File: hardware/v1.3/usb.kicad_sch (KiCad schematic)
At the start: 47 parts, among them J3 USB_C_Receptacle_USB2.0_14P, J4 USB_C_Receptacle_USB2.0_14P, J5 USB_C_Receptacle_USB2.0_14P, U1 ECP5-CABGA256, U6 FT231XQ, U7 TPD2EUSB30A, U8 TPD2EUSB30A, U9 TPD2EUSB30A

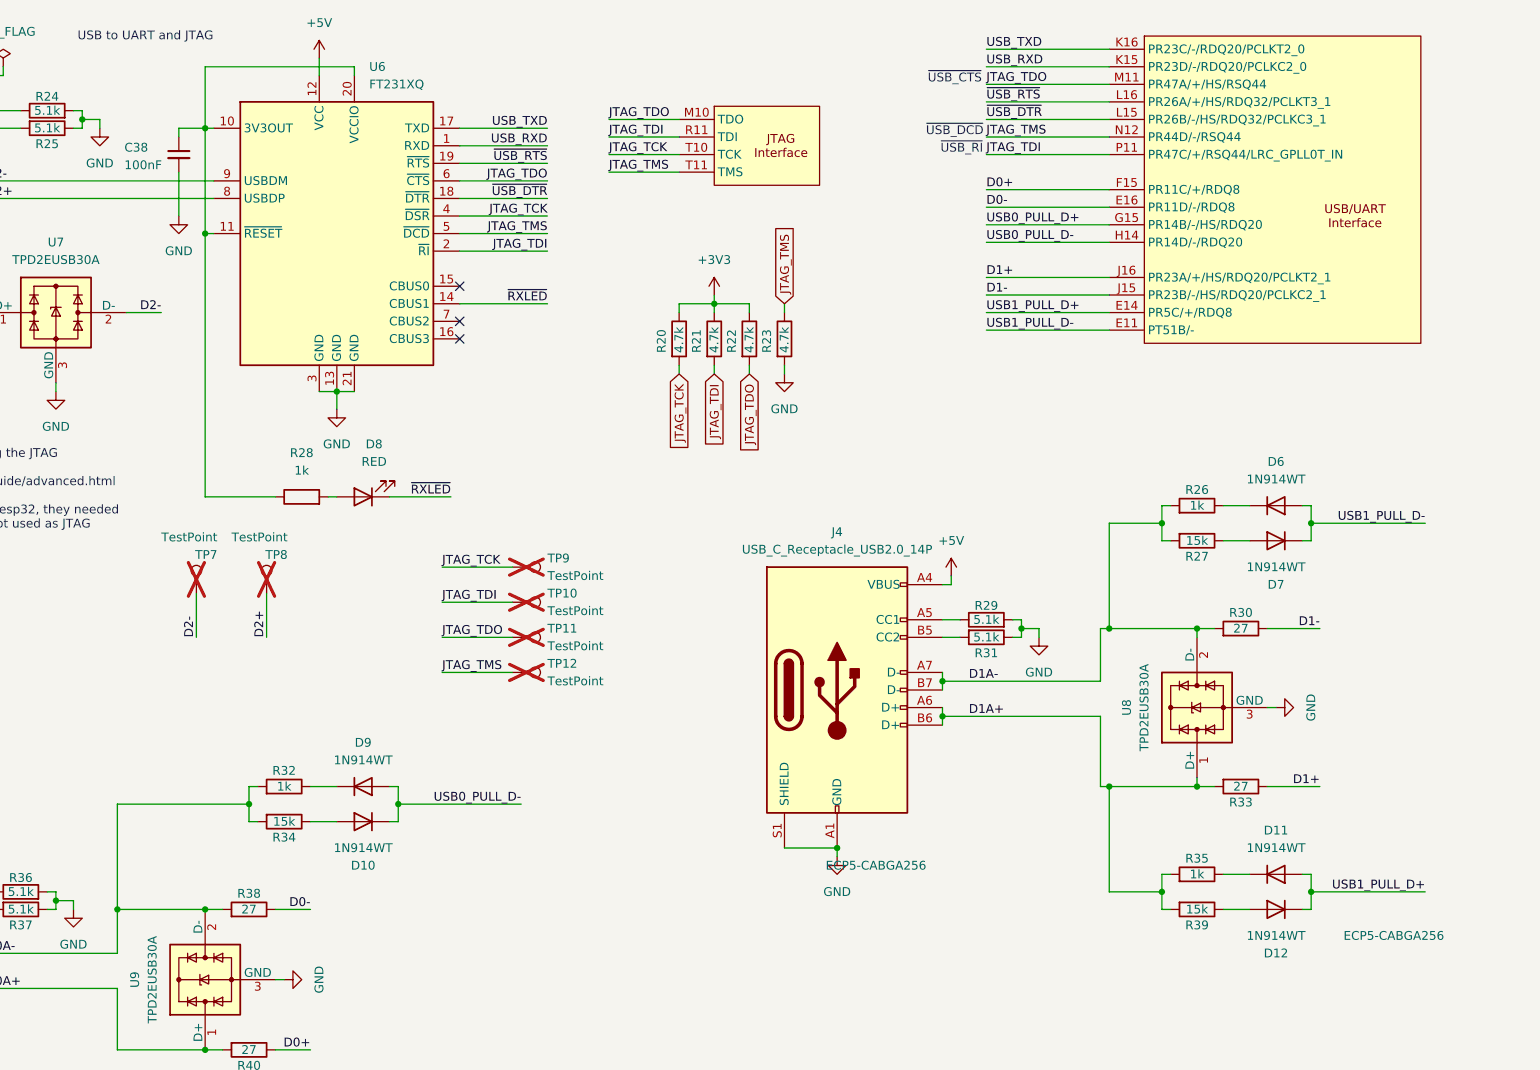
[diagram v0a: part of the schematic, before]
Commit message: Refine README
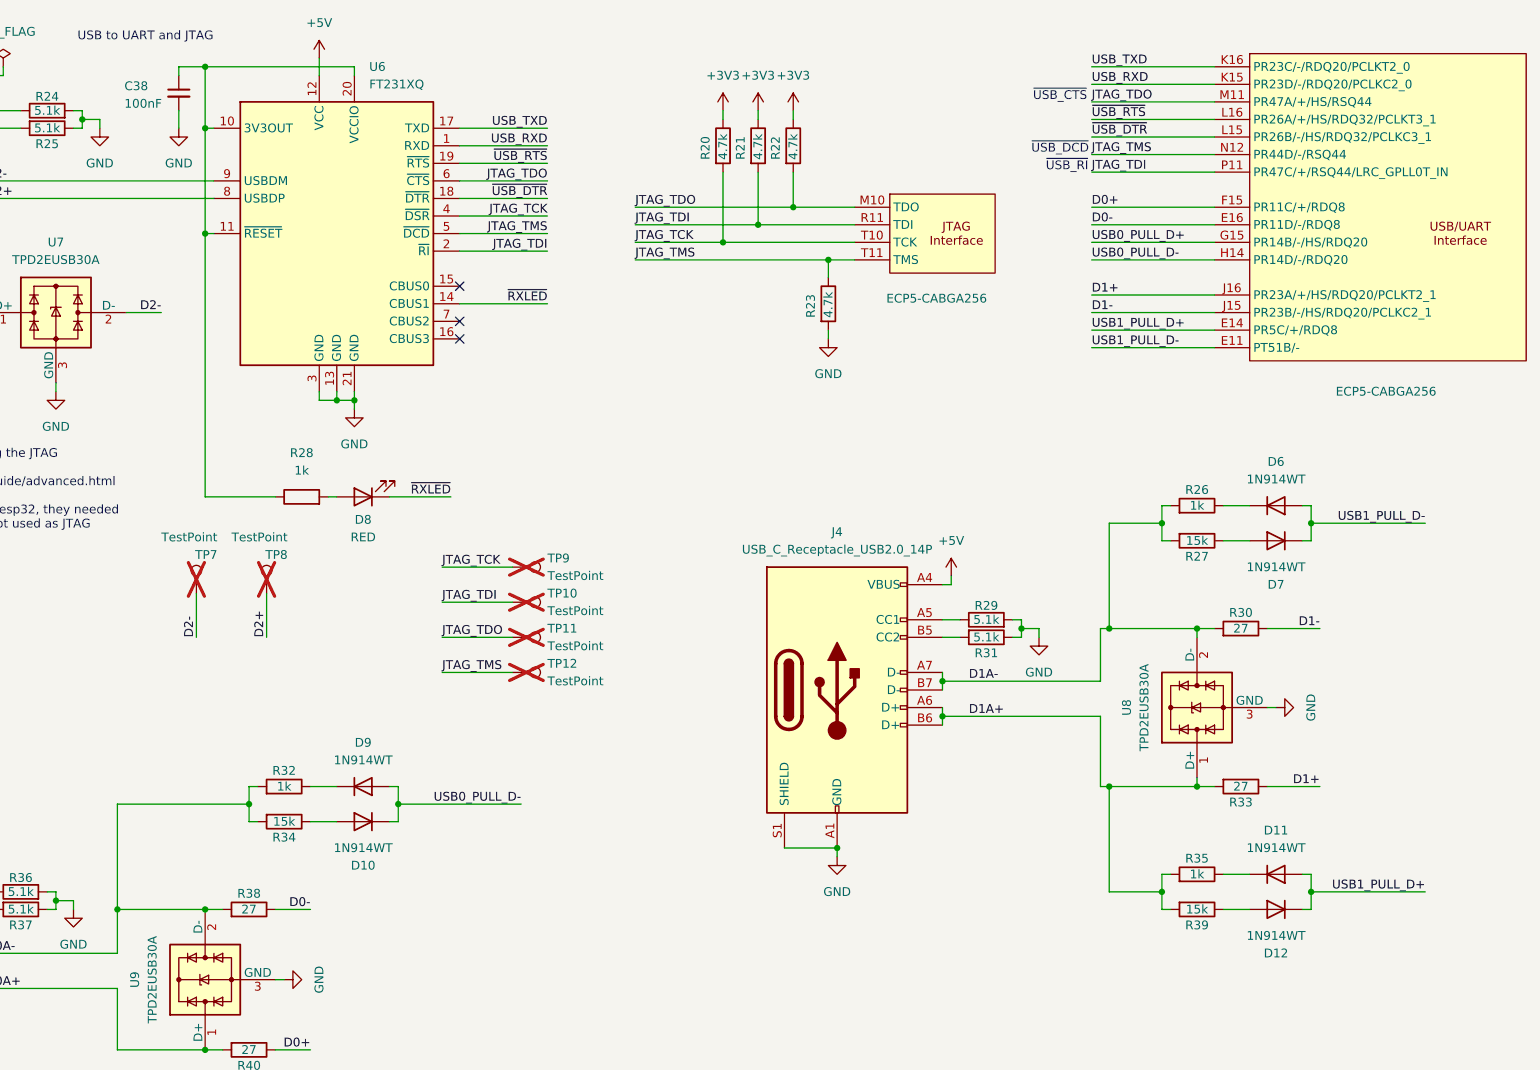
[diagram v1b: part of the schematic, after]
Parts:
- C38: LCSC Link (none) -> https://lcsc.com/product-detail/Multilayer-Ceramic-Capacito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; LCSC Part # C307331 -> C307331; Manufactuer Part Number (none) -> CL05B104KB54PNC
- D10, D11, D12, D13, D14, D6, D7, D9: LCSC Link (none) -> https://lcsc.com/product-detail/Switching-Diodes_CBI-1N914W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; Manufactuer Part Number (none) -> 1N914WT
- D8: LCSC Link (none) -> https://lcsc.com/product-detail/LED-Indication-Discrete_Hub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; LCSC Part # C2286 -> C2286; Manufactuer Part Number (none) -> KT-0603R
- J3, J4, J5: LCSC Link (none) -> https://lcsc.com/product-detail/USB-Connectors_SHOU-HAN-TYP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; Manufactuer Part Number (none) -> TYPE-C 16PIN 2MD(073)
- R20, R21, R22, R23: LCSC Link (none) -> https://lcsc.com/product-detail/Chip-Resistor-Surface-Mount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; LCSC Part # C25900 -> C25900; Manufactuer Part Number (none) -> 0402WGF4701TCE
- R24, R25, R29, R31, R36, R37: LCSC Link (none) -> https://lcsc.com/product-detail/Chip-Resistor-Surface-Mount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; LCSC Part # C25905 -> C25905; Manufactuer Part Number (none) -> 0402WGF5101TCE
- R26, R28, R32, R35, R41: LCSC Link (none) -> https://lcsc.com/product-detail/Chip-Resistor-Surface-Mount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; Manufactuer Part Number (none) -> 0402WGF1001TCE
- R27, R34, R39, R42: LCSC Link (none) -> https://lcsc.com/product-detail/Chip-Resistor-Surface-Mount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; Manufactuer Part Number (none) -> 0402WGF1502TCE
- R30, R33, R38, R40: LCSC Link (none) -> https://lcsc.com/product-detail/Chip-Resistor-Surface-Mount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; Manufactuer Part Number (none) -> 0201WMF270JTEE
- U1: LCSC Link (none) -> https://lcsc.com/product-detail/Programmable-Logic-Device-C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; LCSC Part # (none) -> C1521614; Manufactuer Part Number (none) -> LFE5U-25F-6BG256C
- U6: LCSC Link (none) -> https://lcsc.com/product-detail/USB-Converters_FTDI-FT231XQ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; Manufactuer Part Number (none) -> FT231XQ-R
- U7, U8, U9: LCSC Link (none) -> https://lcsc.com/product-detail/ESD-and-Surge-Protection-TV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; Manufactuer Part Number (none) -> TPD2EUSB30ADRTR
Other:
- moved on the sheet: C38, R20, R21, R22, R23

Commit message: DVI multires
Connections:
- net JTAG_TDI: no longer U1.P11 (PR47C/+/RSQ44/LRC_GPLL0T_IN)
- net JTAG_TDO: no longer U1.M11 (PR47A/+/HS/RSQ44)
- net JTAG_TMS: no longer U1.N12 (PR44D/-/RSQ44)
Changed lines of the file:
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@@
-	(wire
-		(pts
-			(xy 218.44 31.75) (xy 236.22 31.75)
-		)
-		(stroke
-			(width 0)
-			(type default)
-		)
-	)
 	(wire
 		(pts
@@
 		)
 		(stroke
-			(width 0)
-			(type default)
-		)
-	)
-	(wire
-		(pts
-			(xy 218.44 39.37) (xy 236.22 39.37)
-		)
-		(stroke
-			(width 0)
-			(type default)
-		)
-	)
-	(wire
-		(pts
-			(xy 218.44 41.91) (xy 236.22 41.91)
-		)
-		(stroke

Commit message: Update files
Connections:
- no-connect marks 3 -> 6
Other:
- note added: "FPGA-TN-02039 specified pull resistors"
- note added: "The FTDI chip can bitbang the JTAG output on any pin UART: https://umarcor.github.io/openFPGALoader/guide/advanced.html"
- note removed: "The FTDI chip can probably bit bang the JTAG output on any pin: https://umarcor.github.io/openFPGALoader/guide/advanced.html ULX chose the pins because to program their esp32, they needed specific uart outputs, and the ones left got used as JTAG"
- note removed: "~{USB_CTS}"
- note removed: "~{USB_DCD}"
- note removed: "~{USB_RI}"
- moved on the sheet: C38, D10, D11, D12, D13, D14, D6, D7, D8, D9, J3, J4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

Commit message: Update to v1.3 board
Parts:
- TP10, TP11, TP12, TP7, TP8, TP9: now left out of the parts list

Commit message: Final mass production files
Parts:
- added C37: 22uF, Capacitor_SMD:C_0603_1608Metric, symbol Device:C
- TP10, TP11, TP12, TP9: footprint TestPoint:TestPoint_Pad_D1.0mm -> icepi-lib:TestPoint_Pad_D1.0mm_Blank
- TP7, TP8: footprint TestPoint:TestPoint_Pad_D2.0mm -> icepi-lib:TestPoint_Pad_D2.0mm_Blank
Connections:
- net +5V: now also C37.1
- net GND: now also C37.2
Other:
- note added: "PWRin (bulk?) decoupling"
- moved on the sheet: D10, D13, D14, D9, J5, R32, R34, R36, R37, R38, R40, R41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

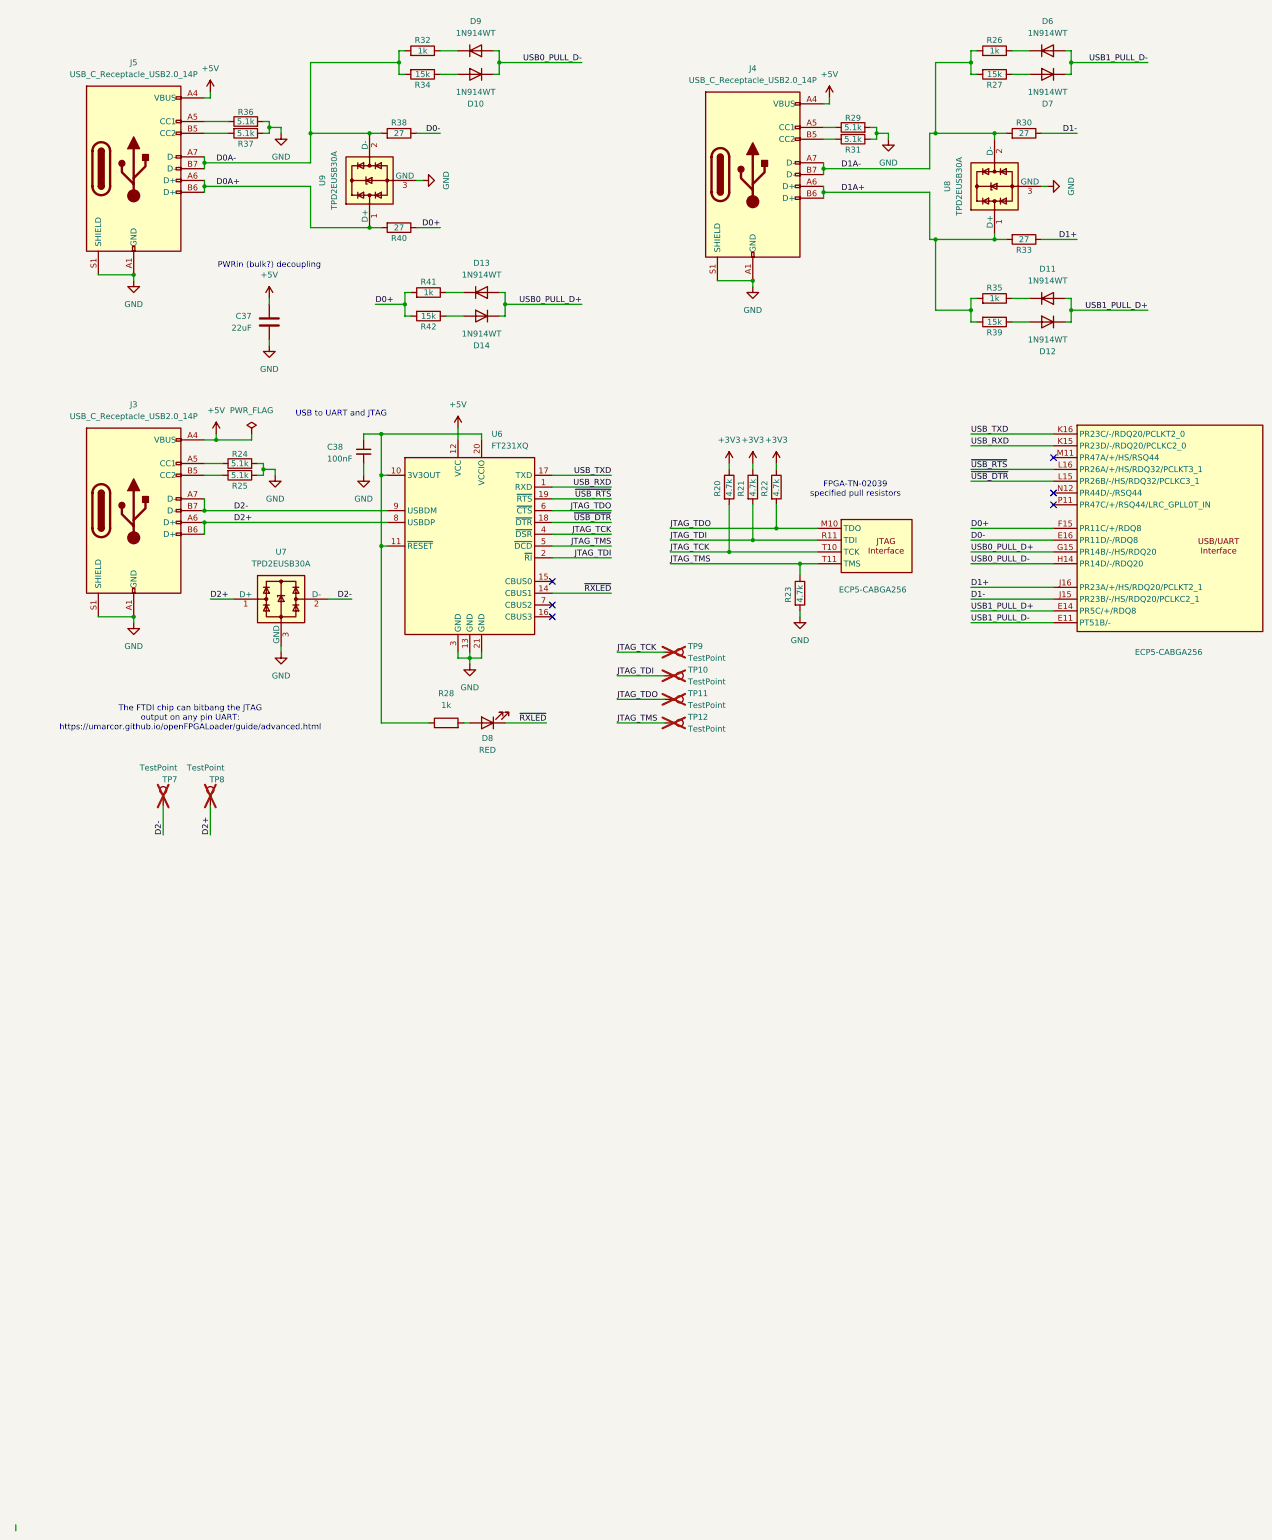
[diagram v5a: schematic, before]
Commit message: Improve makefile and hardware
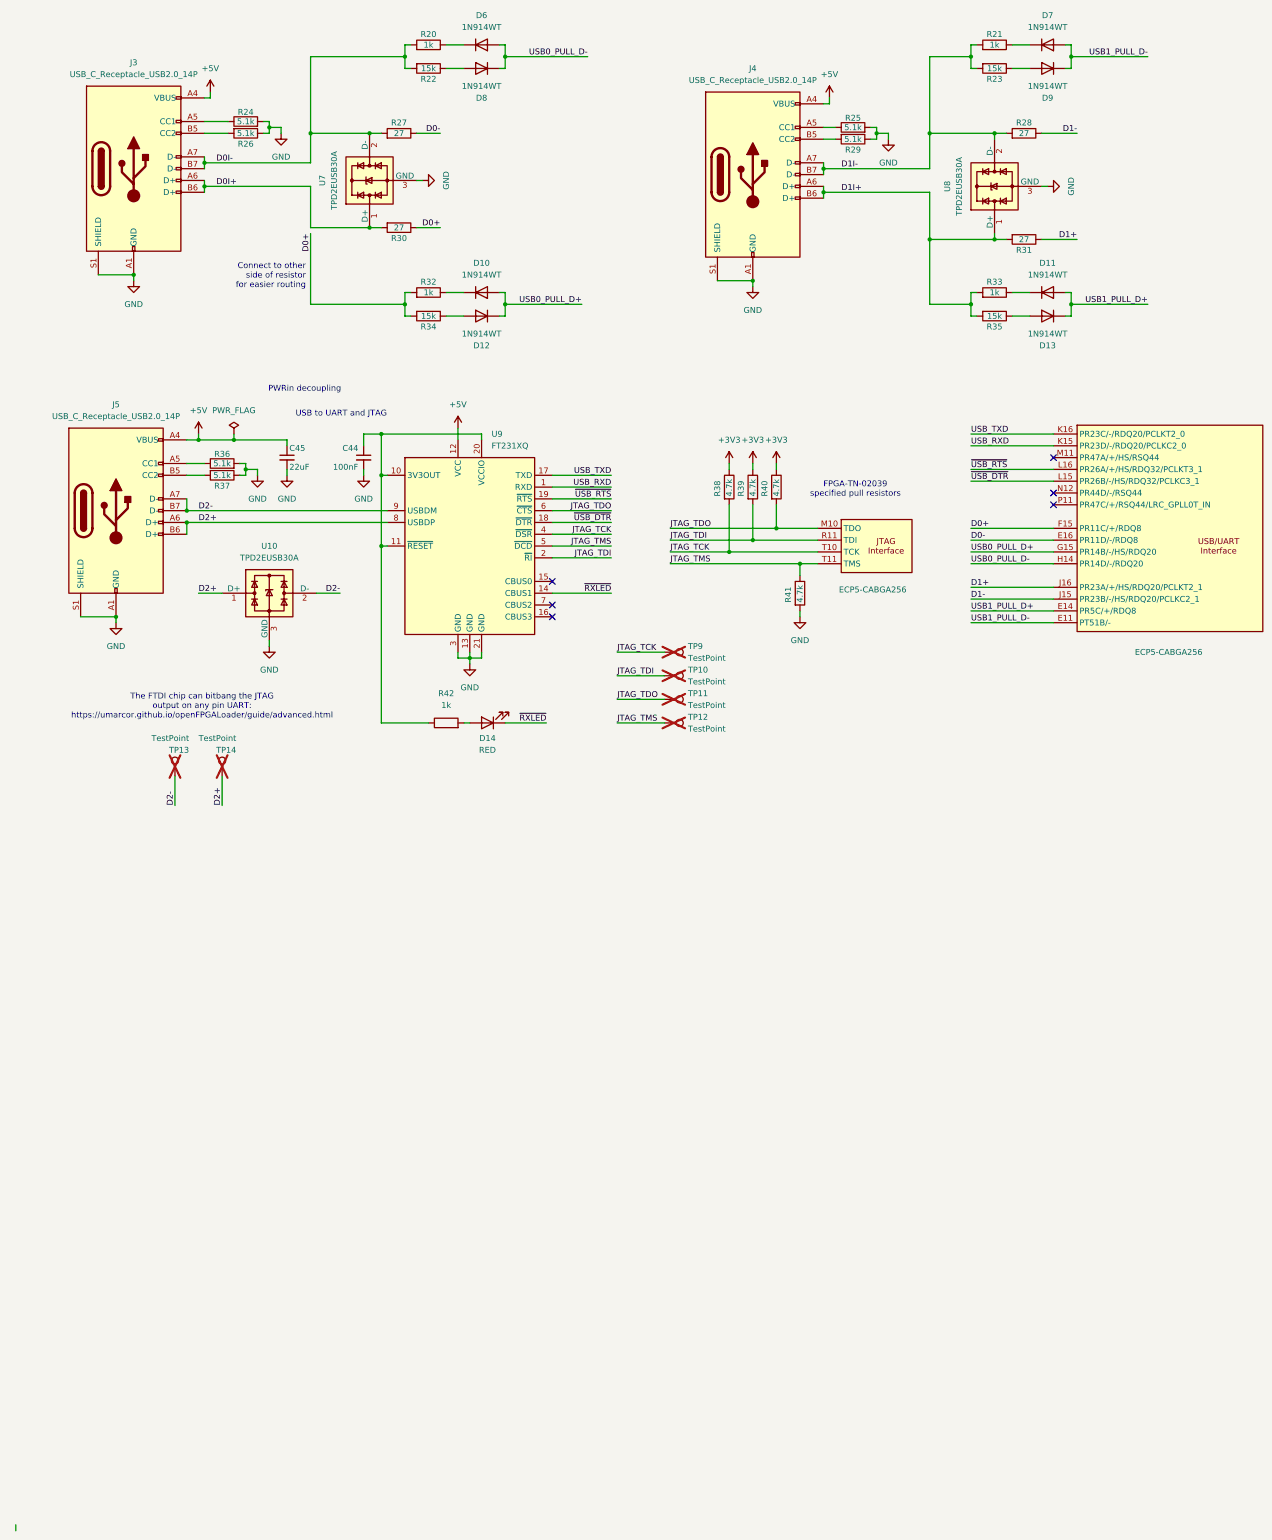
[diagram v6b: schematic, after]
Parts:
- C45: renamed from C37; symbol Device:C -> Device:C_Small
- renumbered C38 to C44, D13 to D10, D14 to D12, D12 to D13, D8 to D14, D9 to D6, D6 to D7, D10 to D8, D7 to D9, J5 to J3, J3 to J5, R32 to R20, R26 to R21, R34 to R22, R27 to R23, R36 to R24, R29 to R25, R37 to R26, R38 to R27, R30 to R28, R31 to R29, R40 to R30, R33 to R31, R41 to R32, R35 to R33, R42 to R34, R39 to R35, R24 to R36, R25 to R37, R20 to R38, R21 to R39, R22 to R40, R23 to R41, R28 to R42, TP7 to TP13, TP8 to TP14, U7 to U10, U9 to U7, U6 to U9
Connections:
- net D0A+ renamed D0I+
- net D0A- renamed D0I-
- net D1A+ renamed D1I+
- net D1A- renamed D1I-
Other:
- note added: "Connect to other side of resistor for easier routing"
- note added: "PWRin decoupling"
- note removed: "PWRin (bulk?) decoupling"
- title: Icepi zero -> Icepi Zero
- moved on the sheet: C44, C45, D11, D13, D6, D7, D8, D9, J5, R20, R21, R22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
